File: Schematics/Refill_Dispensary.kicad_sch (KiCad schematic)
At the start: 28 parts, among them Q1 2N3905, Q2 2N3905, Q3 2N3905, SW1 SW_Push, SW2 SW_Push, SW3 SW_Push, U1 RP2040, U2 Screen, U3 Flash Memory, U5 OPAMP

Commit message: minor changes
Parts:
- removed U2: Screen, Display:NHD-C0220BiZ, symbol Display_Character:NHD-C0220BIZ
- added D1, D2: DIODE, symbol pspice:DIODE
- added R1, R2: R, symbol Device:R
- added U?: UI Screen, Display:NHD-C0220BiZ, symbol Display_Character:NHD-C0220BIZ
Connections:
- net +12V: now also R2.1
- net +3.3V: now also U?.5 (VDD)
- net GND: now also R1.2, U?.4 (VSS)
- net P1: now also U1.39 (GPIO27_ADC1); no longer U1.15 (GPIO12)
- net P2: now also U1.40 (GPIO28_ADC2); no longer U1.16 (GPIO13)
- net P3: now also U1.41 (GPIO29_ADC3); no longer U1.17 (GPIO14)
- net S_SCL: now also U?.2 (SCL)
- net S_SDA: now also U?.3 (SDA)
- new net: R1.1, R2.2
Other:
- note added: "Potentiometers on the UI"
- note removed: "UI Screen"

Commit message: Add files via upload
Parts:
- removed D1, D2, D?: DIODE, symbol pspice:DIODE
- removed J? (x3): Conn_02x01, symbol Connector_Generic:Conn_02x01
- removed Q1, Q2, Q3: 2N3905, Package_TO_SOT_THT:TO-92_Inline, symbol Transistor_BJT:2N3905
- removed R1, R2, R? (x3): R, symbol Device:R
- removed RotPot3: R_Potentiometer, symbol Device:R_Potentiometer
- removed U5: OPAMP, symbol pspice:OPAMP
- removed U?: UI Screen, Display:NHD-C0220BiZ, symbol Display_Character:NHD-C0220BIZ
- added C?: C, symbol Device:C
- added C? (x2): 10u, symbol Device:C
- added C?: 100n, symbol Device:C
- added J: USB_BOOT, symbol Connector_Generic:Conn_01x02
- added J?: USB_B_Micro, symbol Connector:USB_B_Micro
- added J?: Conn_01x03, symbol Connector_Generic:Conn_01x03
- added J?: Barrel_Jack_Switch, symbol Connector:Barrel_Jack_Switch
- added L? (x2): L, symbol Device:L
- added Q? (x2): TIP120, Package_TO_SOT_THT:TO-220-3_Vertical, symbol Transistor_BJT:TIP120
- added R? (x3): 1k, symbol Device:R
- added R? (x5): R, symbol Device:R
- added R?: DNF, symbol Device:R
- added R? (x2): 27, symbol Device:R
- added R?: 1K, symbol Device:R
- added U?: NCP1117-3.3_SOT223, Package_TO_SOT_SMD:SOT-223-3_TabPin2, symbol Regulator_Linear:NCP1117-3.3_SOT223
- added U?: UI Screen, Display:NHD-C0220BiZ, symbol Display_Character:NHD-C0220BIZ
- added U?: INA849, Package_SO:VSSOP-8_3.0x3.0mm_P0.65mm, symbol Amplifier_Instrumentation:INA333xxDGK
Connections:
- net +12V: now also J?.2, J?.3 (Pin_3), Q?.2 (C), Q?.2 (C), U?.7 (V+)
- net +3.3V: now also C?.1, C?.1, R?.1, R?.2, R?.2, R?.2, U?.2 (VO), U?.5 (VDD)
- net ADC0: now also C?.1, R?.2
- net GND: now also C?.2, C?.2, C?.2, C?.2, J.1 (Pin_1), J?.1, J?.5 (GND), J?.6 (Shield), R?.1, R?.1, R?.1, U?.1 (GND), U?.4 (V-), U?.4 (VSS), U?.5 (Ref); no longer D1.1 (K), D2.1 (K), D3.1 (K)
- net SW1: now also R?.1
- net SW2: now also R?.1
- net SW3: now also R?.1
- net S_SCL: now also U?.2 (SCL)
- net S_SDA: now also U?.3 (SDA)
- net V1: now also Q?.1 (B)
- net V2: now also Q?.1 (B)
- net at R?.1: now also D?.1 (K), L?.2 (x2)
- net at D?.2 (A): now also L?.1, Q?.3 (E) (x2)
- net QSPI_SS: now reaches U3.1 (~{CS})
- net QSPI_SS: now also U1.56 (QSPI_SS), R?.2, R?.2
- net QSPI_SD1: now reaches U1.55 (QSPI_SD1), U3.2 (DO(IO1))
- net QSPI_SD2: now reaches U1.54 (QSPI_SD2), U3.3 (IO2)
- net QSPI_SD0: now reaches U1.53 (QSPI_SD0), U3.5 (DI(IO0))
- net QSPI_SD3: now reaches U1.51 (QSPI_SD3), U3.7 (IO3)
- net at U1.46 (USB_DM): now also R?.2
- net at U1.47 (USB_DP): now also R?.2
- net P3: no longer names the net of U1.41 (GPIO29_ADC3)
- new net: C?.1, J?.2 (Pin_2), U?.3 (VI)
- new net: J.2 (Pin_2), R?.1
- new net: D1.1 (K), R?.2
- new net: J?.1 (Pin_1), J?.1 (VBUS)
- new net: R?.1, U?.6
- new net: D3.1 (K), R?.2
- new net: D2.1 (K), R?.2
- new net: R?.1, U?.8 (Rg)
- new net: R?.2, U?.1 (Rg)
- new net Load_cell+: U?.3 (+)
- new net Load_cell-: U?.2 (-)
- new net USB_D+: J?.3 (D+), R?.1
- new net USB_D-: J?.2 (D-), R?.1
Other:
- note added: "Machine Status LEDs"
- note added: "Power Supply"
- note added: "User Interface"
- note added: "Valve Control"
- note removed: "Amplifier, but we will actually use Instrumentation Amplifier from TI"
- note removed: "Machine Status"
- note removed: "Potentiometers on the UI"
- note removed: "We need: 1. Voltage transformer 2. Power supply"
- moved on the sheet: C1, D1, D2, D3, D?, R?, RotPot1, RotPot2, SW1, SW2, SW3, U1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

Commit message: Add files via upload
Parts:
- removed C?: C, symbol Device:C
- removed R?: R, symbol Device:R
- removed U?: UI Screen, Display:NHD-C0220BiZ, symbol Display_Character:NHD-C0220BIZ
- removed U?: INA849, Package_SO:VSSOP-8_3.0x3.0mm_P0.65mm, symbol Amplifier_Instrumentation:INA333xxDGK
- added 10k (x2): R, symbol Device:R
- added 1u: C, symbol Device:C
- added C? (x5): 100n, symbol Device:C
- added C? (x2): 27p, symbol Device:C
- added C? (x2): 1u, symbol Device:C
- added D? (x2): D, symbol Device:D
- added R?: 1k, symbol Device:R
- added U?: AD622, symbol Amplifier_Instrumentation:AD620
- added U?: NHD-C0220BIZ, Display:NHD-C0220BiZ, symbol Display_Character:NHD-C0220BIZ
- added Y?: Crystal, symbol Device:Crystal
- R? (x3): value R -> 1k
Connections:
- net +12V: now also U?.7 (Vs+)
- net +3.3V: now also U1.43 (ADC_AVDD), U1.44 (VREG_IN), U1.48 (USB_VDD), 10k.1, 10k.1, C?.1, C?.1, C?.1, C?.1, D?.1 (K), U?.5 (VDD), U?.9 (A)
- net ADC0: now also D?.1 (K), D?.2 (A), U?.6
- net GND: now also C?.1, C?.1, C?.1, C?.1, C?.2, C?.2, C?.2, C?.2, C?.2, D?.2 (A), U?.10 (K), U?.4 (VSS), U?.4 (Vs-), U?.5 (Ref)
- net Load_cell+: now also U?.2 (-)
- net Load_cell-: now also U?.3 (+)
- net S_SCL: now also 10k.2, U?.2 (SCL)
- net S_SDA: now also 10k.2, U?.3 (SDA)
- net at R?.1: now also U?.8 (Rg)
- net at R?.2: now also U?.1 (Rg)
- net at U1.20 (XIN): now also C?.2, Y?.2
- net at U1.21 (XOUT): now also R?.2
- net at U1.23 (DVDD), U1.50 (DVDD): now also U1.45 (VREG_VOUT), C?.1, C?.2, C?.2
- net Clock0: no longer names the net of U1.35 (GPIO23)
- net V3: no longer names the net of U1.4 (GPIO2)
- new net: C?.2, R?.1, Y?.1
- new net: 1u.1, U?.7 (C1+)
- new net: 1u.2, U?.8 (C1-)
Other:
- moved on the sheet: C1, C?, J, R?, U3

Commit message: hello
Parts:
- removed C? (x4): 100n, symbol Device:C
- removed J?: Conn_01x03, symbol Connector_Generic:Conn_01x03
- removed L? (x2): L, symbol Device:L
- removed R? (x2): R, symbol Device:R
- removed R? (x6): 1k, symbol Device:R
- removed R?: 27, symbol Device:R
- removed RotPot1, RotPot2: R_Potentiometer, symbol Device:R_Potentiometer
- removed SW1, SW2, SW3: SW_Push, symbol Switch:SW_Push
- added C10, C11, C13, C9: 100n, Capacitor_SMD:C_0402_1005Metric, symbol Device:C
- added H1, H2, H3, H4: MountingHole, MountingHole:MountingHole_2.1mm, symbol Mechanical:MountingHole
- added J10: Switch 2, Connector_JST:JST_XH_B2B-XH-AM_1x02_P2.50mm_Vertical, symbol Connector_Generic:Conn_01x02
- added J11: Switch 3, Connector_JST:JST_XH_B2B-XH-AM_1x02_P2.50mm_Vertical, symbol Connector_Generic:Conn_01x02
- added J12: Switch 1, Connector_JST:JST_XH_B2B-XH-AM_1x02_P2.50mm_Vertical, symbol Connector_Generic:Conn_01x02
- added J2: Pot 1, Connector_JST:JST_XH_B3B-XH-AM_1x03_P2.50mm_Vertical, symbol Connector_Generic:Conn_01x03
- added J5: Load Cell Power, TerminalBlock:TerminalBlock_Altech_AK300-2_P5.00mm, symbol Connector:Screw_Terminal_01x02
- added J6: Load Cell Data, TerminalBlock:TerminalBlock_Altech_AK300-2_P5.00mm, symbol Connector:Screw_Terminal_01x02
- added J7: Inductor 1, TerminalBlock:TerminalBlock_Altech_AK300-2_P5.00mm, symbol Connector:Screw_Terminal_01x02
- added J8: Inductor 2, TerminalBlock:TerminalBlock_Altech_AK300-2_P5.00mm, symbol Connector:Screw_Terminal_01x02
- added J9: Pot 2, Connector_JST:JST_XH_B3B-XH-AM_1x03_P2.50mm_Vertical, symbol Connector_Generic:Conn_01x03
- added R1, R2, R3, R4, R5, R6: 1K, Resistor_SMD:R_0201_0603Metric, symbol Device:R
- added R15: 27, Resistor_SMD:R_0805_2012Metric, symbol Device:R
- added SW4: SW_SPDT, Button_Switch_SMD:SW_SPDT_CK-JS102011SAQN, symbol Switch:SW_SPDT
- 10k2, R10: renamed from 10k; footprint (none) -> Resistor_SMD:R_0201_0603Metric
- 1u1: renamed from 1u; footprint (none) -> Capacitor_SMD:C_0201_0603Metric
- C1: footprint (none) -> Capacitor_SMD:C_0402_1005Metric
- C12, C8: renamed from C?; footprint (none) -> Capacitor_SMD:C_0201_0603Metric
- C2, C3: renamed from C?; footprint (none) -> Capacitor_SMD:C_1210_3225Metric
- C4, C7: renamed from C?; footprint (none) -> Capacitor_SMD:C_0402_1005Metric
- C5, C6: renamed from C?; footprint (none) -> Capacitor_SMD:C_0805_2012Metric
- D1, D2, D3: footprint (none) -> LED_THT:LED_D3.0mm
- D4, D5, D6, D7: renamed from D?; footprint (none) -> Diode_THT:D_5W_P5.08mm_Vertical_AnodeUp
- J1: renamed from J?; footprint (none) -> Connector_USB:USB_Micro-AB_Molex_47590-0001
- J3: renamed from J?; footprint (none) -> Connector_BarrelJack:BarrelJack_GCT_DCJ200-10-A_Horizontal
- J4: renamed from J; footprint (none) -> Connector:JWT_A3963_1x02_P3.96mm_Vertical
- R11, R7, R8: renamed from R?; footprint (none) -> Resistor_SMD:R_0201_0603Metric
- R12: renamed from R?; footprint (none) -> Resistor_THT:R_Axial_DIN0204_L3.6mm_D1.6mm_P2.54mm_Vertical
- R9: renamed from R?; footprint (none) -> Resistor_SMD:R_0805_2012Metric
- U5: renamed from U?; footprint (none) -> Amplifier_Instrumentation:AD622
- Y1: renamed from Y?; footprint (none) -> Crystal:Crystal_SMD_SeikoEpson_MA505-2Pin_12.7x5.1mm_HandSoldering
- gave numbers to parts that had none: 4
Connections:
- net +12V: now also J3.1, J5.2 (Pin_2), SW4.3 (C); no longer J3.2
- net +3.3V: now also C10.2, C11.2, C13.2, C9.2, J2.3 (Pin_3), J9.3 (Pin_3), R4.2, R5.2, R6.2; no longer C1.1
- net GND: now also C1.1, D4.1 (K), D5.1 (K), J3.2, C10.1, C11.1, C13.1, C9.1, J10.2 (Pin_2), J11.2 (Pin_2), J12.2 (Pin_2), J2.1 (Pin_1), J5.1 (Pin_1), J7.1 (Pin_1), J8.1 (Pin_1), J9.1 (Pin_1), R2.1, R3.1; no longer C1.2, J3.1
- net Load_cell+: now also J6.2 (Pin_2)
- net Load_cell-: now also J6.1 (Pin_1)
- net P1: now also J2.2 (Pin_2)
- net P2: now also J9.2 (Pin_2)
- net SW1: now also J12.1 (Pin_1), R4.1
- net SW2: now also J10.1 (Pin_1), R5.1
- net SW3: now also J11.1 (Pin_1), R6.1
- net USB_D-: now also R15.1
- net at C7.2, C8.1, U1.23 (DVDD)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: now also C1.2
- net at C2.1, U2.3 (VI): now also SW4.2 (B)
- net at D5.2 (A), Q2.3 (E): now also J8.2 (Pin_2)
- net at D1.1 (K): now also R1.2
- net at J1.1 (VBUS): now also SW4.1 (A)
- net at D4.2 (A), Q1.3 (E): now also J7.2 (Pin_2)
- net at D3.1 (K): now also R3.2
- net at U1.46 (USB_DM): now also R15.2
- net at D2.1 (K): now also R2.2
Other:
- moved on the sheet: J3

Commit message: changes
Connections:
- net GND: now also R1.1
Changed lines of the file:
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@@
-    (stroke (width 0) (type default) (color 0 0 0 0))
-  )
-  (wire (pts (xy 20.32 250.2159) (xy 20.32 251.46))
     (stroke (width 0) (type default) (color 0 0 0 0))
   )
@@
     (stroke (width 0) (type default) (color 0 0 0 0))
   )
+  (wire (pts (xy 20.32 250.19) (xy 20.32 251.46))
+    (stroke (width 0) (type default) (color 0 0 0 0))
+  )

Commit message: I'm cant make a PCB
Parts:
- C14: renamed from 1u1; value C -> 1u
- R10: value R -> 10k
- R13: renamed from 10k2; value R -> 10k
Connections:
- net +12V: now also D4.2 (A), D5.2 (A), J7.2 (Pin_2), J8.2 (Pin_2); no longer Q1.2 (C), Q2.2 (C)
- net GND: now also Q1.3 (E), Q2.3 (E); no longer D4.1 (K), D5.1 (K), J7.1 (Pin_1), J8.1 (Pin_1)
- net LED1: now also U1.15 (GPIO12); no longer U1.8 (GPIO6)
- net LED2: now also U1.16 (GPIO13); no longer U1.9 (GPIO7)
- net LED3: now also U1.17 (GPIO14); no longer U1.11 (GPIO8)
- net S_SCL: now also U1.5 (GPIO3); no longer U1.7 (GPIO5)
- net S_SDA: now also U1.4 (GPIO2); no longer U1.6 (GPIO4)
- net +1V1: now reaches C1.2, C7.2, C8.1, U1.23 (DVDD), U1.45 (VREG_VOUT), U1.50 (DVDD)
- net CLK_IN: now reaches C5.2, U1.20 (XIN), Y1.2
- net CLK_OUT: now reaches R11.2, U1.21 (XOUT)
- new net: D5.1 (K), J8.1 (Pin_1), Q2.2 (C)
- new net: D4.1 (K), J7.1 (Pin_1), Q1.2 (C)
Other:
- moved on the sheet: D4, D5, J7, J8, Q1

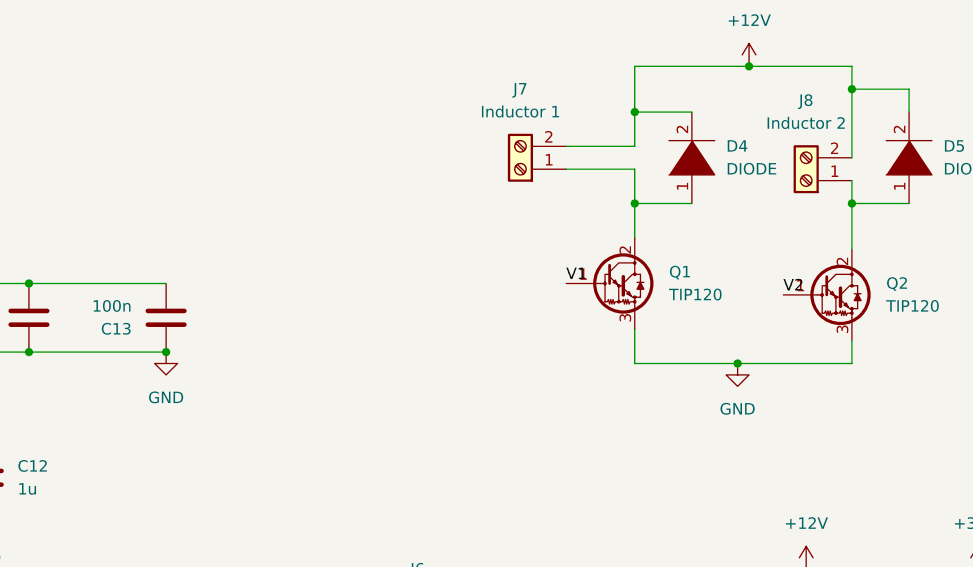
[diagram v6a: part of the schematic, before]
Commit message: board mostly finished
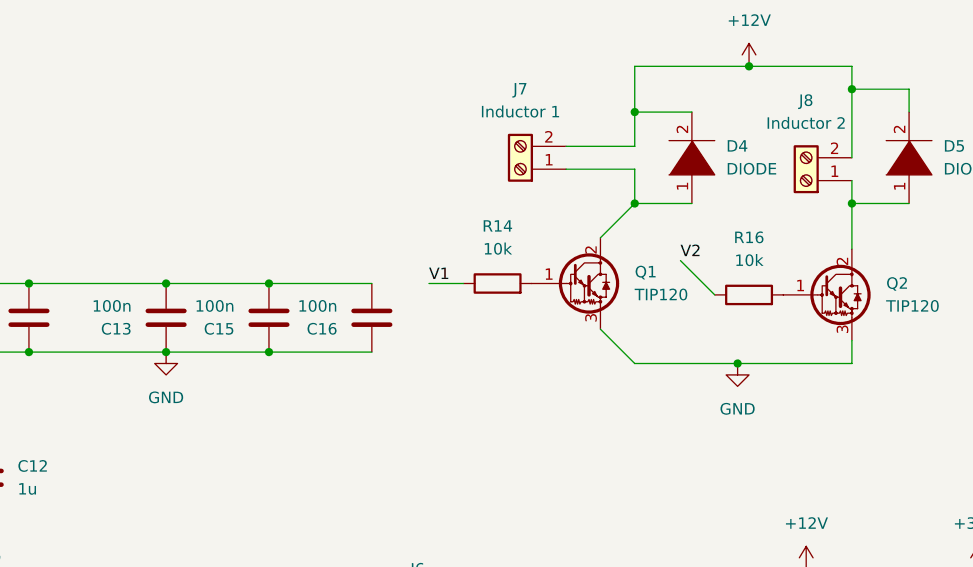
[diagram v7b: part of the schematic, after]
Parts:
- added C15, C16: 100n, Capacitor_SMD:C_0402_1005Metric, symbol Device:C
- added R14, R16: 10k, Resistor_SMD:R_0201_0603Metric, symbol Device:R
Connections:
- net +3.3V: now also C15.2, C16.2
- net GND: now also C15.1, C16.1
- net V1: now also R14.1; no longer Q1.1 (B)
- net V2: now also R16.1; no longer Q2.1 (B)
- new net: Q2.1 (B), R16.2
- new net: Q1.1 (B), R14.2
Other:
- moved on the sheet: Q1
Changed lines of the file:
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@@
   (junction (at 72.39 254) (diameter 0) (color 0 0 0 0)
   )
+  (junction (at 275.59 71.12) (diameter 0) (color 0 0 0 0)
+  )
   (junction (at 264.16 71.12) (diameter 0) (color 0 0 0 0)
   )
@@
   (junction (at 78.74 54.61) (diameter 0) (color 0 0 0 0)
   )
+  (junction (at 264.16 63.5) (diameter 0) (color 0 0 0 0)
+  )
+  (junction (at 275.59 63.5) (diameter 0) (color 0 0 0 0)
+  )
   (junction (at 148.59 111.76) (diameter 0) (color 0 0 0 0)
   )
@@
     (stroke (width 0) (type default) (color 0 0 0 0))
   )
+  (wire (pts (xy 264.16 71.12) (xy 275.59 71.12))
+    (stroke (width 0) (type default) (color 0 0 0 0))
+  )
   (wire (pts (xy 57.15 54.61) (xy 62.23 54.61))
     (stroke (width 0) (type default) (color 0 0 0 0))
@@
     (stroke (width 0) (type default) (color 0 0 0 0))
   )
+  (wire (pts (xy 275.59 63.5) (xy 287.02 63.5))
+    (stroke (width 0) (type default) (color 0 0 0 0))
+  )
   (wire (pts (xy 96.52 236.22) (xy 96.52 240.03))
     (stroke (width 0) (type default) (color 0 0 0 0))
   )
-  (wire (pts (xy 316.23 68.58) (xy 316.23 72.39))
+  (wire (pts (xy 312.42 68.58) (xy 316.23 72.39))
     (stroke (width 0) (type default) (color 0 0 0 0))
   )
@@
     (stroke (width 0) (type default) (color 0 0 0 0))
   )
+  (wire (pts (xy 264.16 63.5) (xy 275.59 63.5))
+    (stroke (width 0) (type default) (color 0 0 0 0))
+  )
   (wire (pts (xy 148.59 100.33) (xy 148.59 111.76))
     (stroke (width 0) (type default) (color 0 0 0 0))
@@
     (stroke (width 0) (type default) (color 0 0 0 0))
   )
+  (wire (pts (xy 293.37 63.5) (xy 297.18 63.5))
+    (stroke (width 0) (type default) (color 0 0 0 0))
+  )
   (wire (pts (xy 125.73 129.54) (xy 135.89 129.54))
     (stroke (width 0) (type default) (color 0 0 0 0))
@@
     (stroke (width 0) (type default) (color 0 0 0 0))
   )
+  (wire (pts (xy 321.31 60.96) (xy 325.12 64.77))
+    (stroke (width 0) (type default) (color 0 0 0 0))
+  )
   (wire (pts (xy 229.87 63.5) (xy 240.03 63.5))
     (stroke (width 0) (type default) (color 0 0 0 0))
@@
     (stroke (width 0) (type default) (color 0 0 0 0))
   )
-  (wire (pts (xy 316.23 54.61) (xy 316.23 58.42))
+  (wire (pts (xy 316.23 54.61) (xy 312.42 58.42))
     (stroke (width 0) (type default) (color 0 0 0 0))
   )
@@
   )
   (wire (pts (xy 172.72 147.32) (xy 176.53 147.32))
+    (stroke (width 0) (type default) (color 0 0 0 0))
+  )
+  (wire (pts (xy 275.59 71.12) (xy 287.02 71.12))
     (stroke (width 0) (type default) (color 0 0 0 0))
   )
@@
     (effects (font (size 1.27 1.27)) (justify left bottom))
   )
-  (label "V1" (at 308.61 63.5 0)
+  (label "V1" (at 293.37 63.5 0)
     (effects (font (size 1.27 1.27)) (justify left bottom))
   )
@@
     (effects (font (size 1.27 1.27)) (justify left bottom))
   )
-  (label "V2" (at 332.74 64.77 0)
+  (label "V2" (at 321.31 60.96 0)
     (effects (font (size 1.27 1.27)) (justify left bottom))
   )
@@
     (pin "2")
   )
+  (symbol (lib_id "Device:C") (at 287.02 67.31 180) (unit 1)
+    (in_bom yes) (on_board yes) (fields_autoplaced)
+    (property "Reference" "C16" (id 0) (at 283.21 68.5801 0)
+      (effects (font (size 1.27 1.27)) (justify left))
+    )
+    (property "Value" "100n" (id 1) (at 283.21 66.0401 0)
+      (effects (font (size 1.27 1.27)) (justify left))
+    )
+    (property "Footprint" "Capacitor_SMD:C_0402_1005Metric" (id 2) (at 286.0548 63.5 0)
+      (effects (font (size 1.27 1.27)) hide)
+    )
+    (property "Datasheet" "~" (id 3) (at 287.02 67.31 0)
+      (effects (font (size 1.27 1.27)) hide)
+    )
+    (pin "1")
+    (pin "2")
+  )
+  (symbol (lib_id "Device:R") (at 328.93 64.77 90) (unit 1)
+    (in_bom yes) (on_board yes) (fields_autoplaced)
+    (property "Reference" "R16" (id 0) (at 328.93 58.42 90))
+    (property "Value" "10k" (id 1) (at 328.93 60.96 90))
+    (property "Footprint" "Resistor_SMD:R_0201_0603Metric" (id 2) (at 328.93 66.548 90)
+      (effects (font (size 1.27 1.27)) hide)
+    )
+    (property "Datasheet" "~" (id 3) (at 328.93 64.77 0)
+      (effects (font (size 1.27 1.27)) hide)
+    )
+    (pin "1")
+    (pin "2")
+  )
   (symbol (lib_id "power:+3.3V") (at 72.39 247.65 0) (unit 1)
     (in_bom yes) (on_board yes) (fields_autoplaced)
@@
     )
     (property "Datasheet" "~" (id 3) (at 180.34 111.76 0)
+      (effects (font (size 1.27 1.27)) hide)
+    )
+    (pin "1")
+    (pin "2")
+  )
+  (symbol (lib_id "Device:C") (at 275.59 67.31 180) (unit 1)
+    (in_bom yes) (on_board yes) (fields_autoplaced)
+    (property "Reference" "C15" (id 0) (at 271.78 68.5801 0)
+      (effects (font (size 1.27 1.27)) (justify left))
+    )
+    (property "Value" "100n" (id 1) (at 271.78 66.0401 0)
+      (effects (font (size 1.27 1.27)) (justify left))
+    )
+    (property "Footprint" "Capacitor_SMD:C_0402_1005Metric" (id 2) (at 274.6248 63.5 0)
+      (effects (font (size 1.27 1.27)) hide)
+    )
+    (property "Datasheet" "~" (id 3) (at 275.59 67.31 0)
       (effects (font (size 1.27 1.27)) hide)
     )
@@
     (pin "2")
   )
+  (symbol (lib_id "Device:R") (at 300.99 63.5 90) (unit 1)
+    (in_bom yes) (on_board yes) (fields_autoplaced)
+    (property "Reference" "R14" (id 0) (at 300.99 57.15 90))
+    (property "Value" "10k" (id 1) (at 300.99 59.69 90))
+    (property "Footprint" "Resistor_SMD:R_0201_0603Metric" (id 2) (at 300.99 65.278 90)
+      (effects (font (size 1.27 1.27)) hide)
+    )
+    (property "Datasheet" "~" (id 3) (at 300.99 63.5 0)
+      (effects (font (size 1.27 1.27)) hide)
+    )
+    (pin "1")
+    (pin "2")
+  )
   (symbol (lib_id "Device:C") (at 168.91 158.75 90) (unit 1)
     (in_bom yes) (on_board yes) (fields_autoplaced)
@@
     (pin "1")
   )
-  (symbol (lib_id "Transistor_BJT:TIP120") (at 313.69 63.5 0) (unit 1)
-    (in_bom yes) (on_board yes) (fields_autoplaced)
-    (property "Reference" "Q1" (id 0) (at 320.04 62.2299 0)
-      (effects (font (size 1.27 1.27)) (justify left))
-    )
-    (property "Value" "TIP120" (id 1) (at 320.04 64.7699 0)
-      (effects (font (size 1.27 1.27)) (justify left))
-    )
-    (property "Footprint" "Package_TO_SOT_THT:TO-220-3_Vertical" (id 2) (at 318.77 65.405 0)
+  (symbol (lib_id "Transistor_BJT:TIP120") (at 309.88 63.5 0) (unit 1)
+    (in_bom yes) (on_board yes) (fields_autoplaced)
+    (property "Reference" "Q1" (id 0) (at 316.23 62.2299 0)
+      (effects (font (size 1.27 1.27)) (justify left))
+    )
+    (property "Value" "TIP120" (id 1) (at 316.23 64.7699 0)
+      (effects (font (size 1.27 1.27)) (justify left))
+    )
+    (property "Footprint" "Package_TO_SOT_THT:TO-220-3_Vertical" (id 2) (at 314.96 65.405 0)
       (effects (font (size 1.27 1.27) italic) (justify left) hide)
     )
-    (property "Datasheet" "https://www.onsemi.com/pub/Collateral/TIP120-D.PDF" (id 3) (at 313.69 63.5 0)
+    (property "Datasheet" "https://www.onsemi.com/pub/Collateral/TIP120-D.PDF" (id 3) (at 309.88 63.5 0)
       (effects (font (size 1.27 1.27)) (justify left) hide)
     )
@@
       (reference "C14") (unit 1) (value "1u") (footprint "Capacitor_SMD:C_0201_0603Metric")
     )
+    (path "/5da68b2b-441d-4c18-9b12-f7569d98980c"
+      (reference "C15") (unit 1) (value "100n") (footprint "Capacitor_SMD:C_0402_1005Metric")
+    )
+    (path "/3be23725-2ddb-47cd-8507-8d5a89bd558d"
+      (reference "C16") (unit 1) (value "100n") (footprint "Capacitor_SMD:C_0402_1005Metric")
+    )
     (path "/1679f79d-ed90-4001-9722-d8e370f5696d"
       (reference "D1") (unit 1) (value "LED") (footprint "LED_THT:LED_D3.0mm")
@@
       (reference "R13") (unit 1) (value "10k") (footprint "Resistor_SMD:R_0201_0603Metric")
     )
+    (path "/ab613322-c3a9-4d10-b0a6-7a236211ab69"
+      (reference "R14") (unit 1) (value "10k") (footprint "Resistor_SMD:R_0201_0603Metric")
+    )
     (path "/5ad17cce-431f-43db-b338-0ed82177f530"
       (reference "R15") (unit 1) (value "27") (footprint "Resistor_SMD:R_0805_2012Metric")
     )
+    (path "/3d35b248-bae3-4f77-9166-a04933351c3f"
+      (reference "R16") (unit 1) (value "10k") (footprint "Resistor_SMD:R_0201_0603Metric")
+    )
     (path "/97d684aa-94d0-49de-b3b8-cdc9d921bb6e"
